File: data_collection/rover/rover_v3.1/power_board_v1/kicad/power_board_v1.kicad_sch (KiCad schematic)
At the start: 41 parts, among them J1 XT60_BATT, J10 from Pi USB2, J2 PANEL_SW, J3 PI5 5.1V (USB-C pigtail), J4 USB_A radio1, J5 USB_A radio2, J6 AUX 5V 2A, J7 PI GPIO harness, J8 AUX_CTL out, J9 from Pi USB1, Q1 SQJ457EP rev-pol, Q2 SQJQ140E, Q3 SQJQ140E, Q4 2N7002 en-drv, U1 LM5146-Q1 stage, U2 LM5146-Q1 stage, U3 ATtiny816, U5 INA226, U6 HT7550 (VBATT->5V mcu), U7 TPS2553 1.7A, U8 TPS2553 1.7A

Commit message: power board schematic: netlist corrections (PFET rev-pol orientation, panel switch to MCU SW_SENSE, USB FAULT decoupled from LOW_BATT)
Co-Authored-By: Claude Fable 5 <noreply@anthropic.com>
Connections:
- net LOW_BATT: no longer U7.5 (FAULT)
- net VBATT_P: now also Q1.2 (S); no longer Q1.3 (D)
- net VBATT_RAW: now also Q1.3 (D); no longer Q1.2 (S)
- net SW_PANEL renamed SW_SENSE
- net SW_SENSE: now also U3.12 (SW_SENSE)

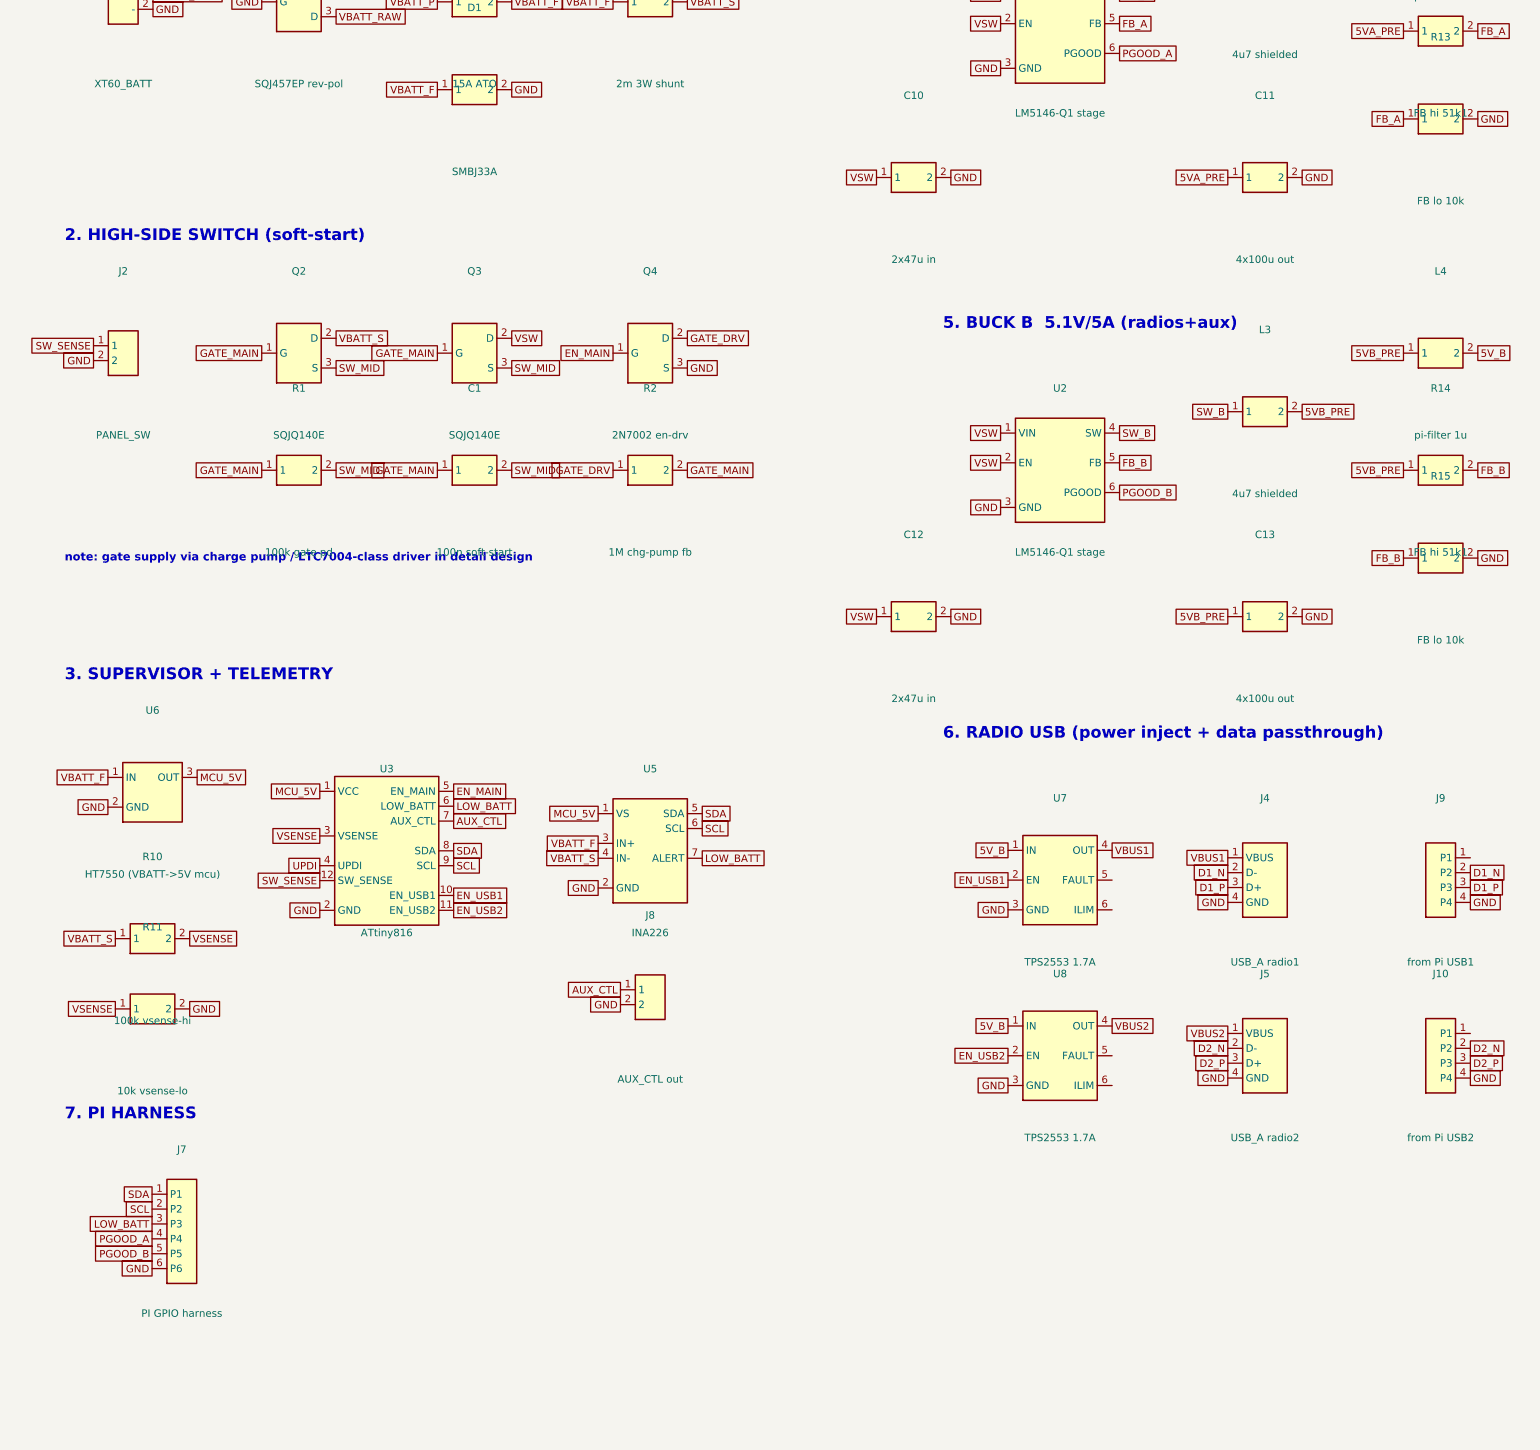
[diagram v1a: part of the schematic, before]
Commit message: power board: production review — 9 findings applied (LDO 60V swap, RILIMs, pullups, ESD, fsw 600kHz), datasheet-pinned BOM, reference-design mapping, A-E checklists + production gates
Co-Authored-By: Claude Fable 5 <noreply@anthropic.com>
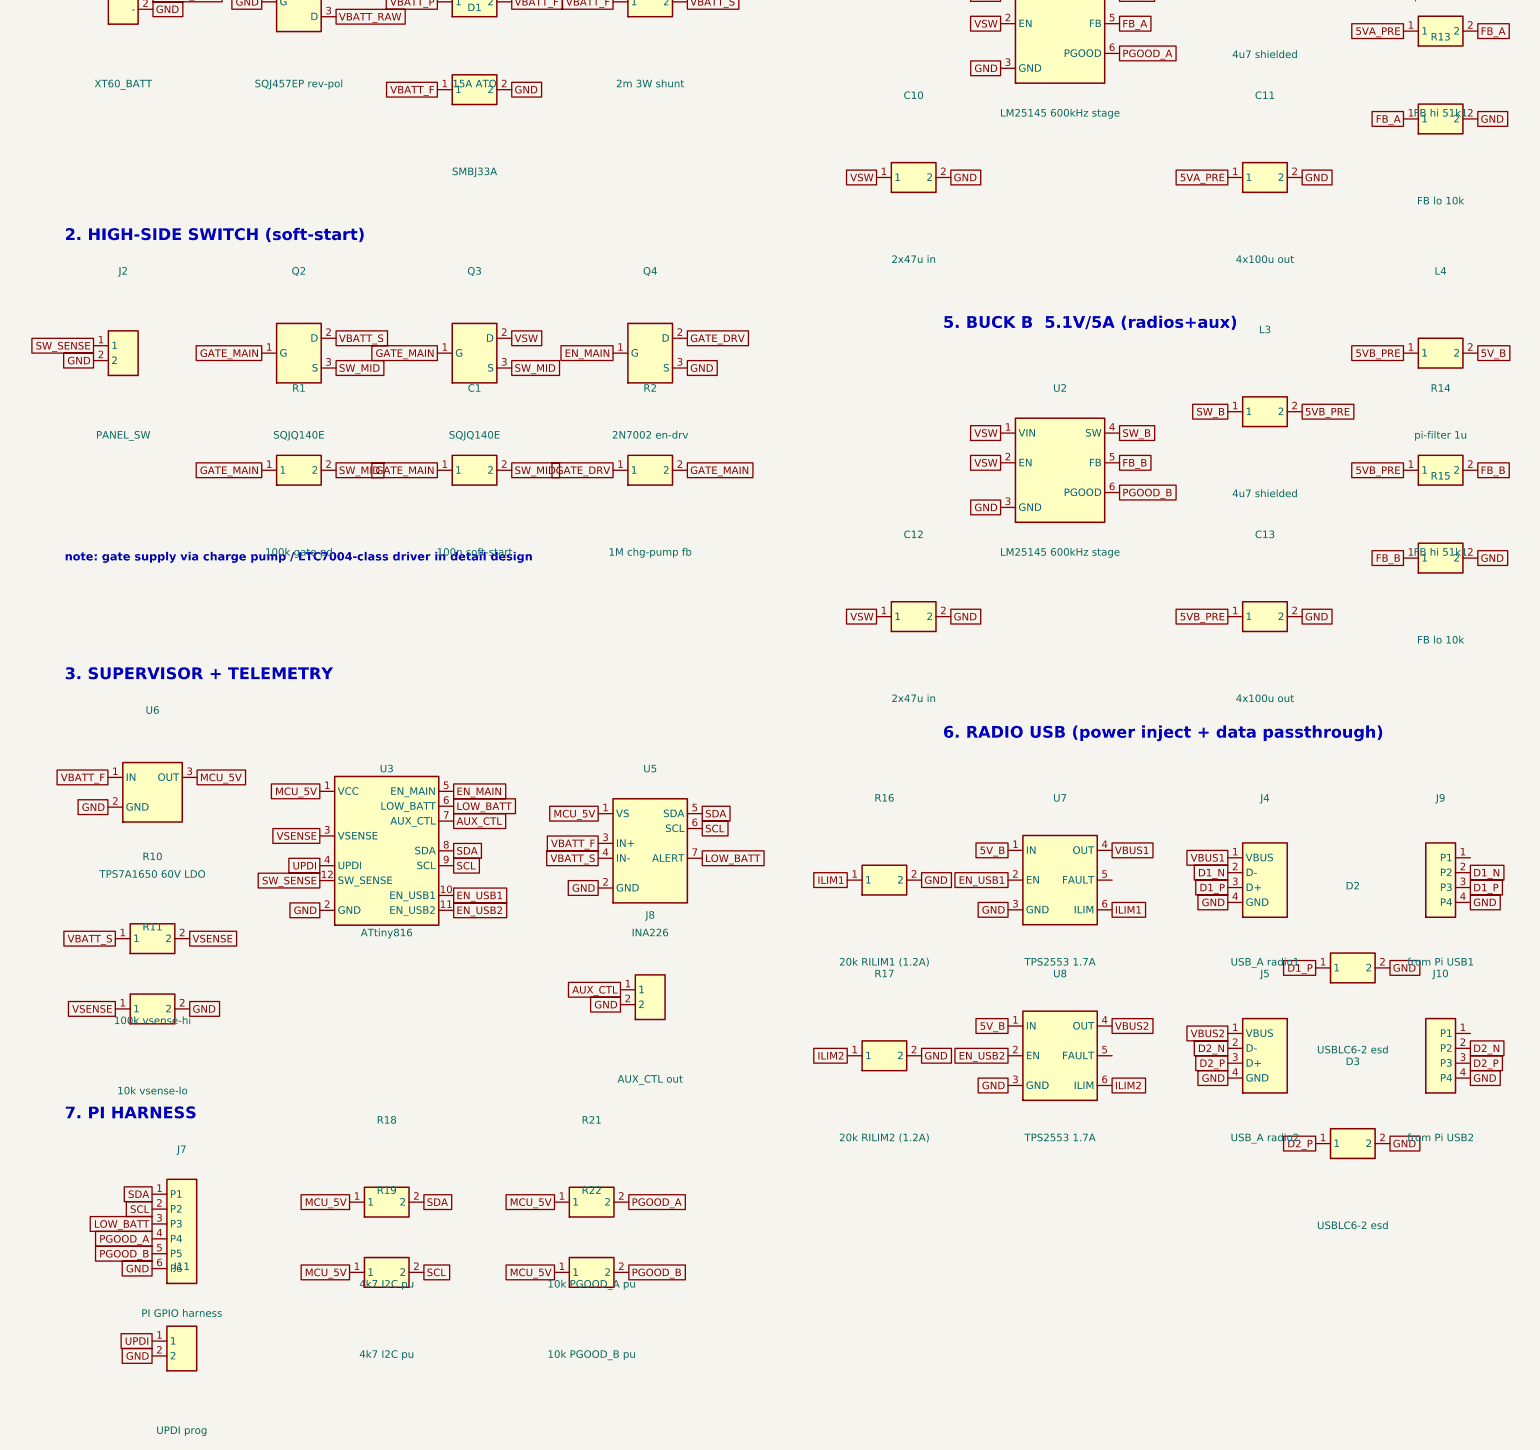
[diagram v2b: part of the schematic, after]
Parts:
- added D2, D3: USBLC6-2 esd, symbol pwr:TVS
- added J11: UPDI prog, symbol pwr:SCREW2
- added R16: 20k RILIM1 (1.2A), symbol pwr:RES
- added R17: 20k RILIM2 (1.2A), symbol pwr:RES
- added R18, R19: 4k7 I2C pu, symbol pwr:RES
- added R21: 10k PGOOD_A pu, symbol pwr:RES
- added R22: 10k PGOOD_B pu, symbol pwr:RES
- U1, U2: value LM5146-Q1 stage -> LM25145 600kHz stage
- U6: value HT7550 (VBATT->5V mcu) -> TPS7A1650 60V LDO
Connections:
- net D1_P: now also D2.1
- net D2_P: now also D3.1
- net GND: now also D2.2, D3.2, J11.2, R16.2, R17.2
- net MCU_5V: now also R18.1, R19.1, R21.1, R22.1
- net PGOOD_A: now also R21.2
- net PGOOD_B: now also R22.2
- net SCL: now also R19.2
- net SDA: now also R18.2
- net UPDI: now also J11.1
- net ILIM1: now reaches U7.6 (ILIM)
- net ILIM1: now also R16.1
- net ILIM2: now reaches U8.6 (ILIM)
- net ILIM2: now also R17.1

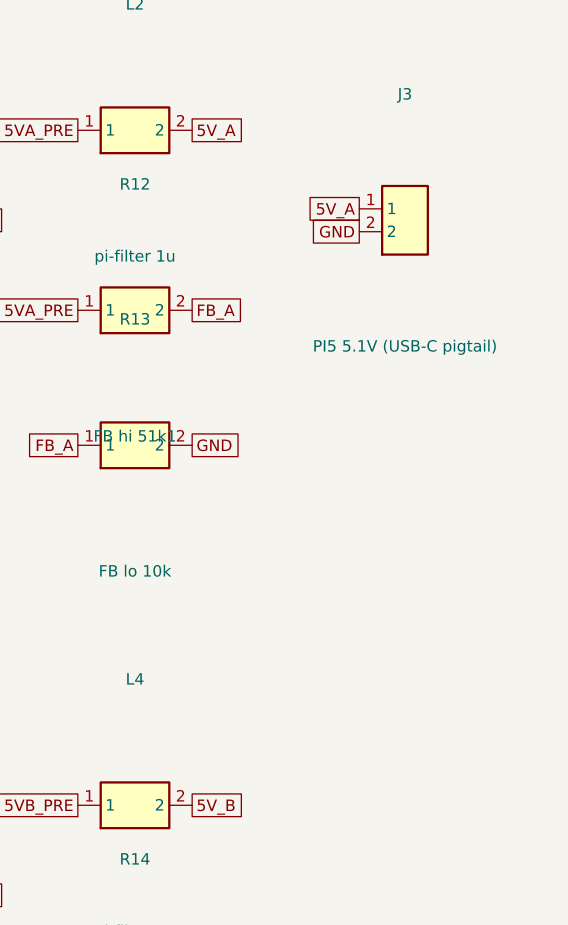
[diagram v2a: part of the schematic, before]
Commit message: P0 decision 3 locked: on-board USB-C receptacle (10k Rp) + specified Silkland 0.5ft 240W cable + XT30 fallback; schematic + docs updated
Co-Authored-By: Claude Fable 5 <noreply@anthropic.com>
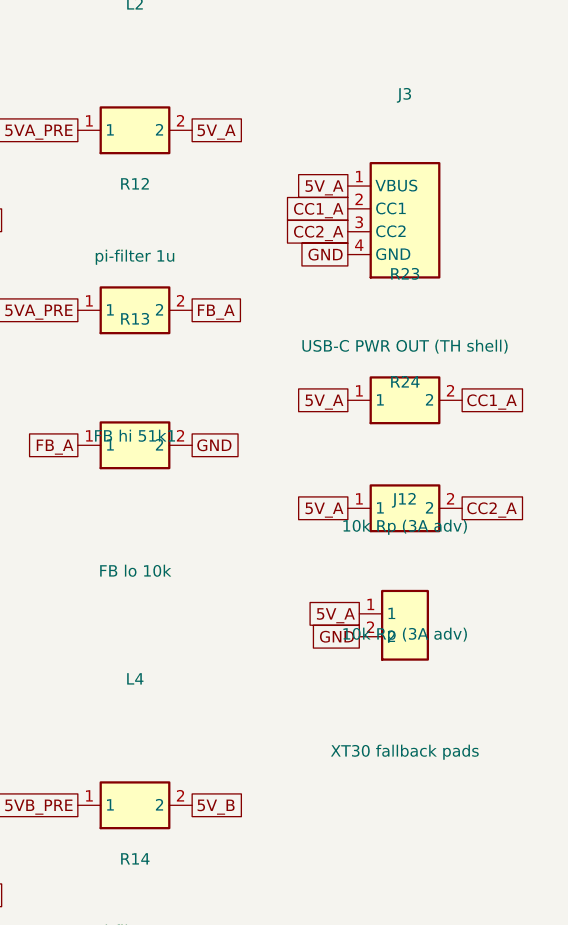
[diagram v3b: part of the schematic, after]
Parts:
- removed J3: PI5 5.1V (USB-C pigtail), symbol pwr:SCREW2
- added J12: XT30 fallback pads, symbol pwr:SCREW2
- added J3: USB-C PWR OUT (TH shell), symbol pwr:USBC_PWR
- added R23, R24: 10k Rp (3A adv), symbol pwr:RES
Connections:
- net 5V_A: now also J12.1, J3.1 (VBUS), R23.1, R24.1
- net GND: now also J12.2, J3.4 (GND)
- new net CC1_A: J3.2 (CC1), R23.2
- new net CC2_A: J3.3 (CC2), R24.2

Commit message: Schematic v2: LM74800-Q1 front-end, fully-expanded LM25145 buck stages (P1 values), 3V3 MCU rail, INA226 on switched side, full ATtiny816 pin map; PLAN/DESIGN synced
Co-Authored-By: Claude Fable 5 <noreply@anthropic.com>
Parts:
- removed C10, C12: 2x47u in, symbol pwr:CAP
- removed C11, C13: 4x100u out, symbol pwr:CAP
- removed J11: UPDI prog, symbol pwr:SCREW2
- removed J7: PI GPIO harness, symbol pwr:HDR6
- removed L1, L3: 4u7 shielded, symbol pwr:IND
- removed Q1: SQJ457EP rev-pol, symbol pwr:PFET
- removed Q4: 2N7002 en-drv, symbol pwr:NFET
- removed R12, R14: FB hi 51k1, symbol pwr:RES
- removed R13, R15: FB lo 10k, symbol pwr:RES
- removed U1, U2: LM25145 600kHz stage, symbol pwr:BUCK_5V1
- removed U6: TPS7A1650 60V LDO, symbol pwr:LDO_5V
- added C2: 100n VS-GND, symbol pwr:CAP
- added C3: 47n HGATE dv/dt (10ms), symbol pwr:CAP
- added C4: 100n vsense hold, symbol pwr:CAP
- added CA1, CB1: 47n SS (4ms), symbol pwr:CAP
- added CA10, CB10: 1n2 CC3, symbol pwr:CAP
- added CA11, CB11: 2x22u pi-out, symbol pwr:CAP
- added CA2, CB2: 2u2 VCC, symbol pwr:CAP
- added CA3, CB3: 100n BST, symbol pwr:CAP
- added CA4: 18p CILIM, symbol pwr:CAP
- added CA5, CB5: 3x10u 50V in, symbol pwr:CAP
- added CA6, CB6: 4x47u 10V out, symbol pwr:CAP
- added CA7, CB7: 220u poly 25mR, symbol pwr:CAP
- added CA8, CB8: 8n2 CC1, symbol pwr:CAP
- added CA9, CB9: 39p CC2, symbol pwr:CAP
- added CB4: 22p CILIM, symbol pwr:CAP
- added D4: green status, symbol pwr:LED
- added J11: UPDI prog (UPDI/3V3/GND), symbol pwr:HDR3
- added J7: PI GPIO harness, symbol pwr:HDR8
- added LA1, LB1: 3u3 10A shielded, symbol pwr:IND
- added QA1, QB1: 40V <10mR HS, symbol pwr:NFET
- added QA2, QB2: 40V <8mR LS, symbol pwr:NFET
- added R25: 30k v5a-hi, symbol pwr:RES
- added R26: 10k v5a-lo, symbol pwr:RES
- added R27: 10k NTC-top (3V3_SW), symbol pwr:RES
- added R28: 10k NTC 3380K, symbol pwr:RES
- added R29: 1k LED, symbol pwr:RES
- added R3: 82k5 ladder-bot, symbol pwr:RES
- added R30: 10k FAULT pu, symbol pwr:RES
- added R4: 100k EN-A hi (8.5V on), symbol pwr:RES
- added R5: 16k5 EN-A lo (7.5V off), symbol pwr:RES
- added RA1, RB1: 16k5 RT (606kHz), symbol pwr:RES
- added RA2: 348R RILIM (7A valley), symbol pwr:RES
- added RA3, RB3: 20k RFB1, symbol pwr:RES
- added RA4, RB4: 3k74 RFB2, symbol pwr:RES
- added RA5, RB5: 13k RC1, symbol pwr:RES
- added RA6, RB6: 4k64 RC2, symbol pwr:RES
- added RB2: 287R RILIM (5.7A valley), symbol pwr:RES
- added U1: LM25145 5.1V rail A, symbol pwr:LM25145
- added U2: LM25145 5.1V rail B, symbol pwr:LM25145
- added U4: LM74800-Q1, symbol pwr:LM74800
- added U6: TPS7A16 3V3 60V LDO, symbol pwr:LDO
- added U9: AP2112K-3.3 (switched), symbol pwr:LDO
- C1: value 100n soft-start -> 100n CAP-VS
- D1: value SMBJ33A -> SMBJ16A
- J8: value AUX_CTL out -> AUX_CTL out (JST-GH)
- Q2: value SQJQ140E -> SQJQ140E-A diode
- Q3: value SQJQ140E -> SQJQ140E-B switch
- R1: value 100k gate pd -> 887k ladder-top
- R10: value 100k vsense-hi -> 680k vsense-hi
- R11: value 10k vsense-lo -> 100k vsense-lo
- R2: value 1M chg-pump fb -> 28k7 ladder-mid
- U5: value INA226 -> INA226 (addr 0x40)
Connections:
- net VBATT_P is gone; now on net VBATT_RAW: F1.1
- net 5VA_PRE: now also CA10.1, CA6.1, CA7.1, LA1.2, RA3.1
- net 5VB_PRE: now also CB10.1, CB6.1, CB7.1, LB1.2, RB3.1
- net 5V_A: now also CA11.1, R25.1
- net 5V_B: now also CB11.1, U9.1 (IN)
- net AUX_CTL: now also U3.14 (PB3/AUX_CTL); no longer U3.7 (AUX_CTL)
- net EN_USB1: now also U3.17 (PA1/USB_EN1); no longer U3.10 (EN_USB1)
- net EN_USB2: now also U3.18 (PA2/USB_EN2); no longer U3.11 (EN_USB2)
- net FB_A: now also CA8.2, CA9.2, RA3.2, RA4.1, RA6.2, U1.14 (FB)
- net FB_B: now also CB8.2, CB9.2, RB3.2, RB4.1, RB6.2, U2.14 (FB)
- net GND: now also C2.2, C4.2, CA1.2, CA11.2, CA2.2, CA4.2, CA5.2, CA6.2, CA7.2, CB1.2, CB11.2, CB2.2, CB4.2, CB5.2, CB6.2, CB7.2, D4.2 (K), J11.3 (P3), J7.7 (P7), J7.8 (P8), QA2.3 (S), QB2.3 (S), R26.2, R28.2, R3.2, R5.2, RA1.2, RA4.2, RB1.2, RB4.2, U1.6 (SYNCIN), U1.7 (AGND), U1.8 (PGND), U2.6 (SYNCIN), U2.7 (AGND), U2.8 (PGND), U4.7 (GND), U6.2 (GND), U9.2 (GND)
- net LOW_BATT: now also U3.13 (PC2/LOW_BATT), J7.3 (P3); no longer U3.6 (LOW_BATT), U5.7 (ALERT)
- net PGOOD_A: now also U3.10 (PC0/PGOOD_A), J7.5 (P5), U1.16 (PGOOD), U2.2 (EN)
- net PGOOD_B: now also U3.20 (PC1/PGOOD_B), J7.6 (P6), U2.16 (PGOOD)
- net SCL: now also U3.16 (PB0/SCL), J7.2 (P2); no longer U3.9 (SCL)
- net SDA: now also U3.15 (PB1/SDA), J7.1 (P1); no longer U3.8 (SDA)
- net SW_A: now also CA3.2, LA1.1, QA1.3 (S), QA2.2 (D), RA2.2, U1.12 (SW)
- net SW_B: now also CB3.2, LB1.1, QB1.3 (S), QB2.2 (D), RB2.2, U2.12 (SW)
- net SW_SENSE: now also U3.8 (PB2/SW_SENSE); no longer U3.12 (SW_SENSE)
- net UPDI: now also U3.3 (PA0/UPDI), J11.1 (P1); no longer U3.4 (UPDI)
- net VBATT_F: now also U6.1 (IN)
- net VBATT_S: now also Q2.3 (S), U4.2 (A), U4.3 (VSNS); no longer Q2.2 (D)
- net VSENSE: now also U3.4 (PA4/VIN_SENSE), C4.1; no longer U3.3 (VSENSE)
- net VSW: now also Q3.3 (S), C3.2, CA5.1, CB5.1, QA1.2 (D), QB1.2 (D), R4.1, U1.1 (VIN), U2.1 (VIN), U4.9 (OUT); no longer Q3.2 (D)
- net FAULT_USB: now reaches U8.5 (FAULT)
- net FAULT_USB: now also U3.7 (PA5/FAULT_USB), U7.5 (FAULT), R30.2
- net EN_MAIN renamed V5A_SENSE
- net V5A_SENSE: now also R25.2, R26.1
- net GATE_DRV renamed FE_EN
- net FE_EN: now also R1.2, U3.11 (PB4/FE_EN), U4.6 (EN_UVLO)
- removed net GATE_MAIN: C1.1, Q2.1 (G), Q3.1 (G), R1.1, R2.2
- net MCU_5V renamed MCU_3V3
- net MCU_3V3: now also J11.2 (P2), R30.1, U6.3 (OUT); no longer U5.1 (VS)
- removed net SW_MID: C1.2, Q2.3 (S), Q3.3 (S), R1.2
- new net 3V3_SW: R27.1, U5.1 (VS), U9.3 (OUT)
- new net BST_A: CA3.1, U1.10 (BST)
- new net BST_B: CB3.1, U2.10 (BST)
- new net COMP_A: CA9.1, RA5.1, U1.15 (COMP)
- new net COMP_B: CB9.1, RB5.1, U2.15 (COMP)
- new net CX_A: CA8.1, RA5.2
- new net CX_B: CB8.1, RB5.2
- new net CY_A: CA10.2, RA6.1
- new net CY_B: CB10.2, RB6.1
- new net DG_FE: Q2.1 (G), U4.1 (DGATE)
- new net EN_A: R4.2, R5.1, U1.2 (EN), U3.12 (PB5/BUCKA_EN)
- new net FE_CAP: C1.1, U4.11 (CAP)
- new net FE_LAD: R1.1, U4.4 (SW)
- new net FE_MID: C1.2, C2.1, Q2.2 (D), Q3.2 (D), U4.10 (VS), U4.12 (C)
- new net FE_OV: R2.2, R3.1, U4.5 (OV)
- new net HG_FE: C3.1, Q3.1 (G), U4.8 (HGATE)
- new net HO_A: QA1.1 (G), U1.11 (HO)
- new net HO_B: QB1.1 (G), U2.11 (HO)
- new net ILIM_A: CA4.1, RA2.1, U1.5 (ILIM)
- new net ILIM_B: CB4.1, RB2.1, U2.5 (ILIM)
- new net LED_K: D4.1 (A), R29.2
- new net LED_STAT: R29.1, U3.19 (PA3/LED)
- new net LO_A: QA2.1 (G), U1.13 (LO)
- new net LO_B: QB2.1 (G), U2.13 (LO)
- new net NTC: R27.2, R28.1, U3.6 (PA7/NTC)
- new net RT_A: RA1.1, U1.3 (RT)
- new net RT_B: RB1.1, U2.3 (RT)
- new net SHDN_ACK: J7.4 (P4), U3.9 (PC3/SHDN_ACK)
- new net SS_A: CA1.1, U1.4 (SS)
- new net SS_B: CB1.1, U2.4 (SS)
- new net VCC_A: CA2.1, U1.9 (VCC)
- new net VCC_B: CB2.1, U2.9 (VCC)
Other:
- note added: "1. INPUT + PROTECTION (3S: 9-13V)"
- note added: "2. FRONT-END: LM74800-Q1 + SQJQ140E b2b (rev-pol + on/off + OV; 2.87uA off)"
- note added: "3. SUPERVISOR (always-on ~25uA) + TELEMETRY (switched)"
- note added: "4. BUCK A 5.1V/6A (Pi 5) [values: P1_DETAIL_DESIGN.md sec 2]"
- note added: "5. BUCK B 5.1V/5A (radios+aux) — EN = PGOOD_A (Pi rail first)"
- note added: "7. PI HARNESS (JST-GH) + UPDI"
- note removed: "1. INPUT + PROTECTION"
- note removed: "2. HIGH-SIDE SWITCH (soft-start)"
- note removed: "3. SUPERVISOR + TELEMETRY"
- note removed: "4. BUCK A 5.1V/6A (Pi 5)"
- note removed: "5. BUCK B 5.1V/5A (radios+aux)"
- note removed: "7. PI HARNESS"
- note removed: "note: gate supply via charge pump / LTC7004-class driver in detail design"
